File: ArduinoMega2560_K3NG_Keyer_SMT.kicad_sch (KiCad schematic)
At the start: 5 parts, among them J2 Barrel_Jack, J23 Conn_01x02

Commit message: Small drawing cleanups.
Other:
- sheet Misc: file untitled.kicad_sch -> misc.kicad_sch
- note added: "Arduino Mega 2560 clone Microprocessor"
- note added: "Miscellaneous Parts on separate sheets"
- note removed: "Miscellaneous Parts on separate sheet"
- title: Arduino Mega2560 K3NG Morse Code Keyer - SMT version -> Arduino Mega2560 K3NG Keyer - Microprocessor
- moved on the sheet: A1, JP1

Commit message: Changed power jack and LCD symbols.
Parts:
- removed J2: Barrel_Jack, symbol Connector:Barrel_Jack
- added J2: Conn_01x02, symbol Connector_Generic:Conn_01x02
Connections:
- net GND: now also J2.2 (Pin_2)
- net Vin: now also J2.1 (Pin_1)
- net A3 renamed PS2_DATA
- net D3 renamed PS2_CLK
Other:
- note added: "+"
- note added: "GND"
- note removed: "PS/2 Keyboard"
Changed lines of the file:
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@@
   (junction (at 97.79 156.21) (diameter 0) (color 0 0 0 0)
   )
-  (wire (pts (xy 41.91 31.75) (xy 48.26 31.75))
+  (wire (pts (xy 39.37 31.75) (xy 45.72 31.75))
     (stroke (width 0) (type default))
   )
@@
     (stroke (width 0) (type default))
   )
-  (wire (pts (xy 41.91 36.83) (xy 48.26 36.83))
+  (wire (pts (xy 39.37 34.29) (xy 45.72 34.29))
     (stroke (width 0) (type default))
   )
@@
     (stroke (width 0) (type default))
   )
-  (wire (pts (xy 48.26 36.83) (xy 48.26 39.37))
+  (wire (pts (xy 45.72 34.29) (xy 45.72 36.83))
     (stroke (width 0) (type default))
   )
@@
     (effects (font (size 3 3) (thickness 0.6) bold) (justify left bottom))
   )
-  (text "PS/2 Keyboard" (at 170.18 53.34 0)
+  (text "+" (at 30.48 33.02 0)
     (effects (font (size 1.27 1.27)) (justify left bottom))
   )
@@
     (effects (font (size 1.27 1.27)) (justify left bottom))
   )
-  (text "7-12V" (at 20.32 35.56 0)
-    (effects (font (size 1.27 1.27)) (justify left bottom))
+  (text "7-12V" (at 20.32 34.29 0)
+    (effects (font (size 1.27 1.27) (thickness 0.254) bold) (justify left bottom))
   )
   (text "Notes:\n1. Closeing Solder Jumper JP1 allows +5v from Arduino Mega to power the rest of the circuit.\n2. Paddle DIT also connected to D52 for Straight Key."
@@
     (effects (font (size 1.27 1.27)) (justify left bottom))
   )
-  (text "PS/2 Keyboard" (at 77.47 91.44 0)
+  (text "GND" (at 27.94 35.56 0)
     (effects (font (size 1.27 1.27)) (justify left bottom))
   )
@@
     )
   )
+  (global_label "PS2_CLK" (shape input) (at 163.83 52.07 0) (fields_autoplaced)
+    (effects (font (size 1.27 1.27)) (justify left))
+    (property "Intersheetrefs" "${INTERSHEET_REFS}" (at 175.0399 52.07 0)
+      (effects (font (size 1.27 1.27)) (justify left) hide)
+    )
+  )
   (global_label "DIT" (shape input) (at 163.83 57.15 0) (fields_autoplaced)
     (effects (font (size 1.27 1.27)) (justify left))
@@
     )
   )
-  (global_label "D3" (shape input) (at 163.83 52.07 0) (fields_autoplaced)
-    (effects (font (size 1.27 1.27)) (justify left))
-    (property "Intersheetrefs" "${INTERSHEET_REFS}" (at 169.2947 52.07 0)
-      (effects (font (size 1.27 1.27)) (justify left) hide)
-    )
-  )
   (global_label "LCD_RS" (shape input) (at 163.83 120.65 0) (fields_autoplaced)
     (effects (font (size 1.27 1.27)) (justify left))
@@
     )
   )
-  (global_label "A3" (shape input) (at 97.79 90.17 180) (fields_autoplaced)
-    (effects (font (size 1.27 1.27)) (justify right))
-    (property "Intersheetrefs" "${INTERSHEET_REFS}" (at 92.5067 90.17 0)
+  (global_label "PS2_DATA" (shape input) (at 97.79 90.17 180) (fields_autoplaced)
+    (effects (font (size 1.27 1.27)) (justify right))
+    (property "Intersheetrefs" "${INTERSHEET_REFS}" (at 85.7334 90.17 0)
       (effects (font (size 1.27 1.27)) (justify right) hide)
     )
@@
     )
   )
-  (global_label "Vin" (shape input) (at 48.26 31.75 0) (fields_autoplaced)
-    (effects (font (size 1.27 1.27)) (justify left))
-    (property "Intersheetrefs" "${INTERSHEET_REFS}" (at 54.0876 31.75 0)
+  (global_label "Vin" (shape input) (at 45.72 31.75 0) (fields_autoplaced)
+    (effects (font (size 1.27 1.27)) (justify left))
+    (property "Intersheetrefs" "${INTERSHEET_REFS}" (at 51.5476 31.75 0)
       (effects (font (size 1.27 1.27)) (justify left) hide)
     )
@@
     )
   )
-  (symbol (lib_id "power:GND") (at 97.79 163.83 0) (unit 1)
-    (in_bom yes) (on_board yes) (dnp no) (fields_autoplaced)
-    (property "Reference" "#PWR01" (at 97.79 170.18 0)
-      (effects (font (size 1.27 1.27)) hide)
-    )
-    (property "Value" "GND" (at 97.79 168.91 0)
-      (effects (font (size 1.27 1.27)) hide)
-    )
-    (property "Footprint" "" (at 97.79 163.83 0)
-      (effects (font (size 1.27 1.27)) hide)
-    )
-    (property "Datasheet" "" (at 97.79 163.83 0)
-      (effects (font (size 1.27 1.27)) hide)
-    )
-    (pin "1")
-    (instances
-      (project "ArduinoMega2560_K3NG_Keyer_SMT"
-        (path "/9104ccff-1306-44aa-b78d-6ce3da0acd2a"
-          (reference "#PWR01") (unit 1)
-        )
-      )
-    )
-  )
-  (symbol (lib_id "Connector:Barrel_Jack") (at 34.29 34.29 0) (unit 1)
+  (symbol (lib_id "Connector_Generic:Conn_01x02") (at 34.29 31.75 0) (mirror y) (unit 1)
     (in_bom yes) (on_board yes) (dnp no)
     (property "Reference" "J2" (at 34.29 29.21 0)
       (effects (font (size 1.27 1.27)))
     )
-    (property "Value" "Barrel_Jack" (at 34.29 39.37 0)
-      (effects (font (size 1.27 1.27)))
-    )
-    (property "Footprint" "" (at 35.56 35.306 0)
-      (effects (font (size 1.27 1.27)) hide)
-    )
-    (property "Datasheet" "~" (at 35.56 35.306 0)
+    (property "Value" "Conn_01x02" (at 34.29 27.94 0)
+      (effects (font (size 1.27 1.27)) hide)
+    )
+    (property "Footprint" "" (at 34.29 31.75 0)
+      (effects (font (size 1.27 1.27)) hide)
+    )
+    (property "Datasheet" "~" (at 34.29 31.75 0)
       (effects (font (size 1.27 1.27)) hide)
     )
@@
         (path "/9104ccff-1306-44aa-b78d-6ce3da0acd2a"
           (reference "J2") (unit 1)
+        )
+      )
+    )
+  )
+  (symbol (lib_id "power:GND") (at 97.79 163.83 0) (unit 1)
+    (in_bom yes) (on_board yes) (dnp no) (fields_autoplaced)
+    (property "Reference" "#PWR01" (at 97.79 170.18 0)
+      (effects (font (size 1.27 1.27)) hide)
+    )
+    (property "Value" "GND" (at 97.79 168.91 0)
+      (effects (font (size 1.27 1.27)) hide)
+    )
+    (property "Footprint" "" (at 97.79 163.83 0)
+      (effects (font (size 1.27 1.27)) hide)
+    )
+    (property "Datasheet" "" (at 97.79 163.83 0)
+      (effects (font (size 1.27 1.27)) hide)
+    )
+    (pin "1")
+    (instances
+      (project "ArduinoMega2560_K3NG_Keyer_SMT"
+        (path "/9104ccff-1306-44aa-b78d-6ce3da0acd2a"
+          (reference "#PWR01") (unit 1)
         )
       )
@@
     )
   )
-  (symbol (lib_id "power:GND") (at 48.26 39.37 0) (unit 1)
+  (symbol (lib_id "power:GND") (at 45.72 36.83 0) (unit 1)
     (in_bom yes) (on_board yes) (dnp no) (fields_autoplaced)
-    (property "Reference" "#PWR04" (at 48.26 45.72 0)
-      (effects (font (size 1.27 1.27)) hide)
-    )
-    (property "Value" "GND" (at 48.26 44.45 0)
-      (effects (font (size 1.27 1.27)) hide)
-    )
-    (property "Footprint" "" (at 48.26 39.37 0)
-      (effects (font (size 1.27 1.27)) hide)
-    )
-    (property "Datasheet" "" (at 48.26 39.37 0)
-      (effects (font (size 1.27 1.27)) hide)
-    )
+    (property "Reference" "#PWR04" (at 45.72 43.18 0)
+      (effects (font (size 1.27 1.27)) hide)
+    )
+    (property "Value" "GND" (at 45.72 41.91 0)
+      (effects (font (size 1.27 1.27)) hide)
+    )
+    (property "Footprint" "" (at 45.72 36.83 0)
+      (effects (font (size 1.27 1.27)) hide)
+    )
+    (property "Datasheet" "" (at 45.72 36.83 0)
+      (effects (font (size 1.27 1.27)) hide)
+    )

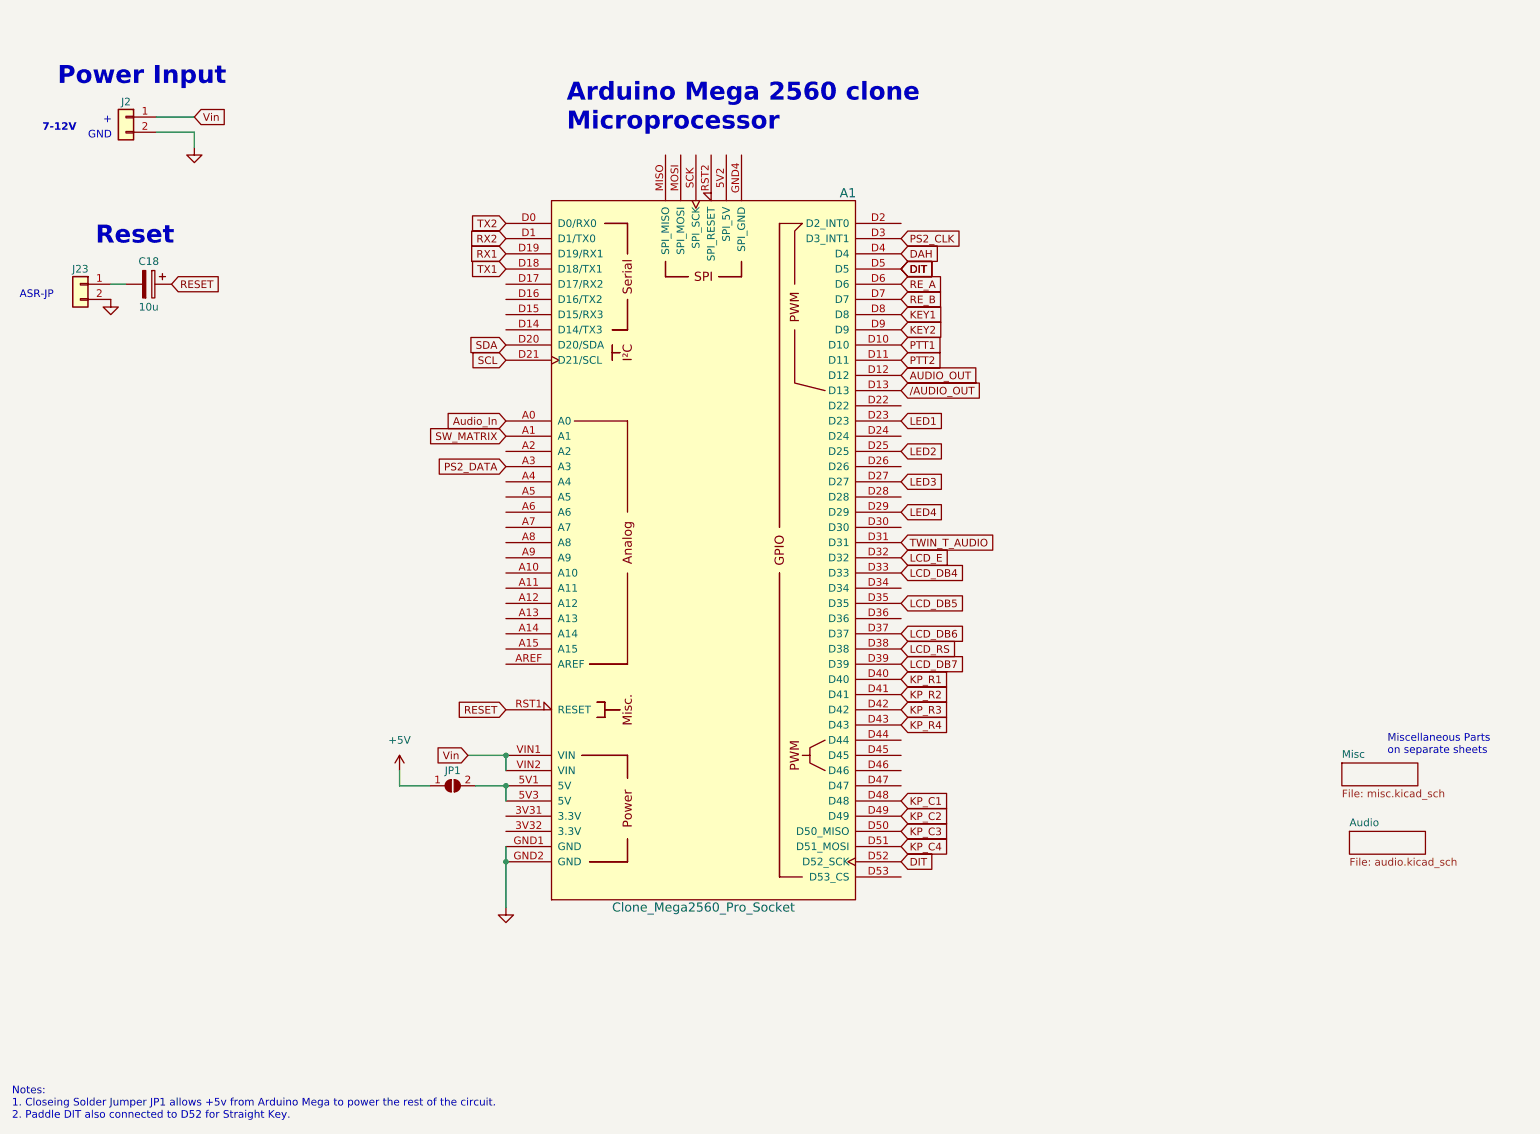
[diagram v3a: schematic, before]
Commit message: Added multi-hole strips to unused pins on Arduino Mega 2560 microprocessor. Also, some minor changes.
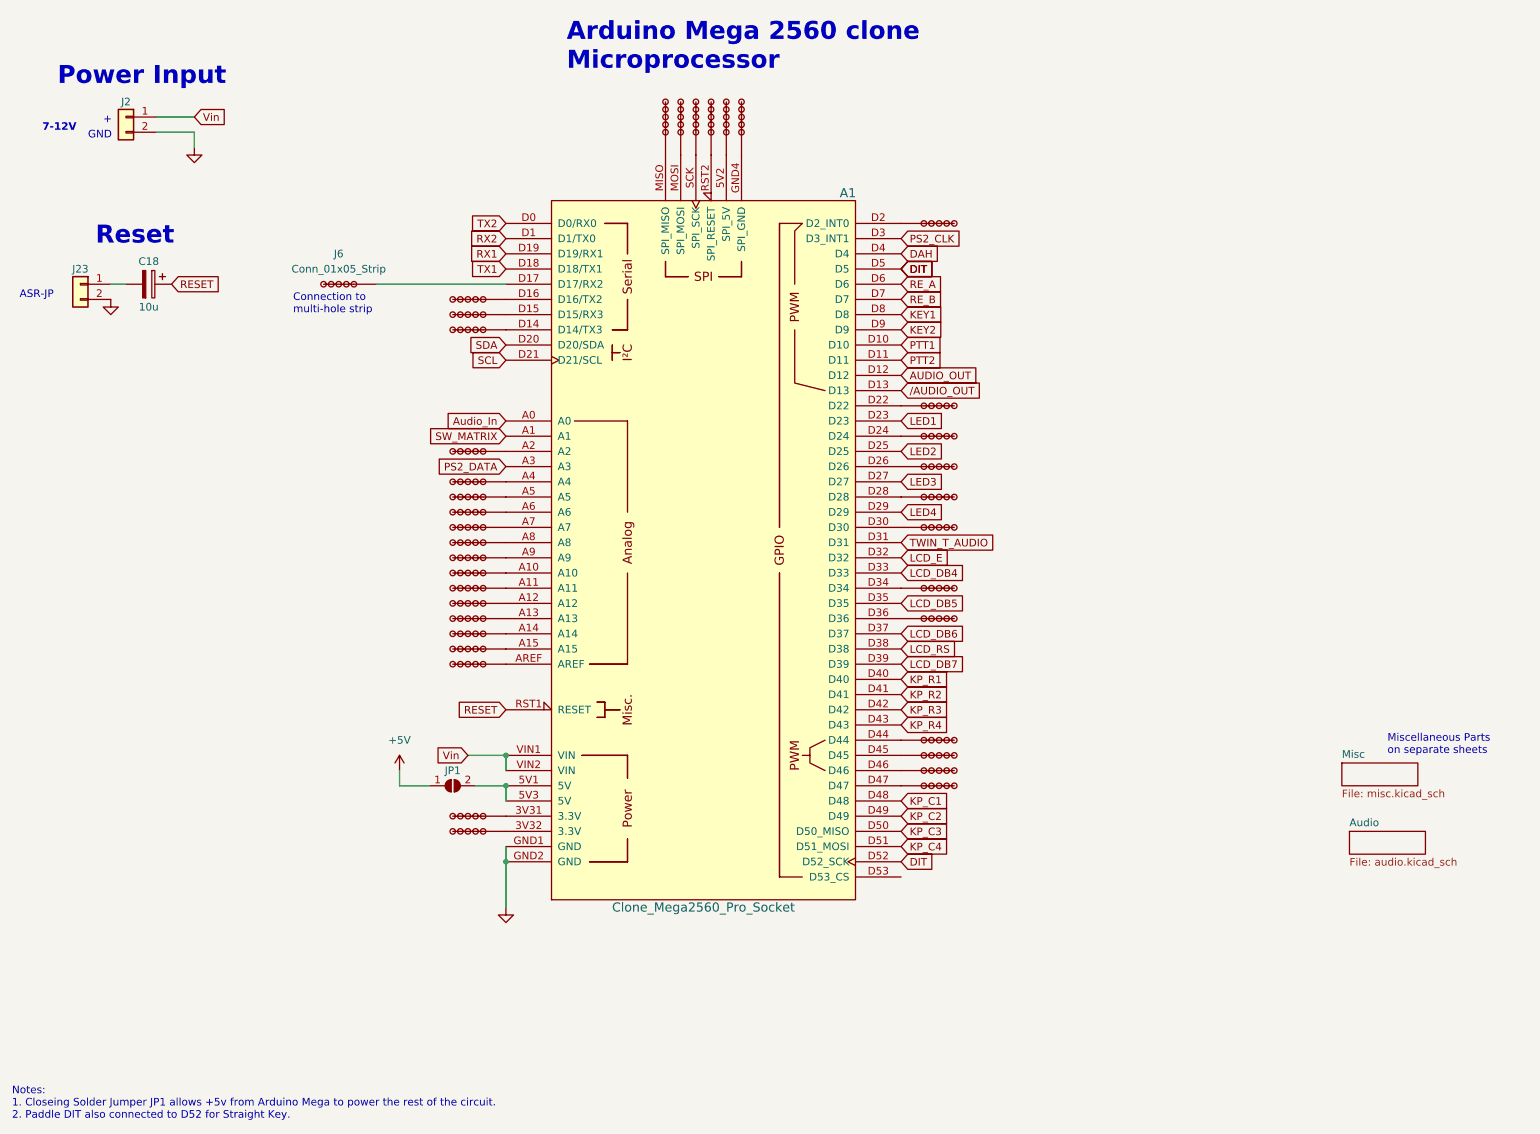
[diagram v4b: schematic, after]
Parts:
- added J10, J11, J12, J13, J25, J26, J27, J28, J29, J30, J31, J32, J33, J34, J35, J36, J37, J38, J39, J40, J41, J42, J43, J44, J45, J46, J47, J48, J49, J50, J51, J52, J53, J54, J6, J7, J8, J9: Conn_01x05_Strip, User:01x05_Strip, symbol User_KICAD6:Conn_01x05_Strip
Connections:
- net at A1.3V31 (3.3V): now also J35. (Pin_1)
- net at A1.3V32 (3.3V): now also J36. (Pin_1)
- net at A1.5V2 (SPI_5V): now also J50. (Pin_1)
- net at A1.A10: now also J28. (Pin_1)
- net at A1.A11: now also J29. (Pin_1)
- net at A1.A12: now also J30. (Pin_1)
- net at A1.A13: now also J31. (Pin_1)
- net at A1.A14: now also J32. (Pin_1)
- net at A1.A15: now also J33. (Pin_1)
- net at A1.A2: now also J10. (Pin_1)
- net at A1.A4: now also J11. (Pin_1)
- net at A1.A5: now also J12. (Pin_1)
- net at A1.A6: now also J13. (Pin_1)
- net at A1.A7: now also J25. (Pin_1)
- net at A1.A8: now also J26. (Pin_1)
- net at A1.A9: now also J27. (Pin_1)
- net at A1.AREF: now also J34. (Pin_1)
- net at A1.D14 (D14/TX3): now also J9. (Pin_1)
- net at A1.D15 (D15/RX3): now also J8. (Pin_1)
- net at A1.D16 (D16/TX2): now also J7. (Pin_1)
- net at A1.D17 (D17/RX2): now also J6. (Pin_1)
- net at A1.D2 (D2_INT0): now also J48. (Pin_1)
- net at A1.D22: now also J47. (Pin_1)
- net at A1.D24: now also J46. (Pin_1)
- net at A1.D26: now also J45. (Pin_1)
- net at A1.D28: now also J44. (Pin_1)
- net at A1.D30: now also J43. (Pin_1)
- net at A1.D34: now also J42. (Pin_1)
- net at A1.D36: now also J41. (Pin_1)
- net at A1.D44: now also J40. (Pin_1)
- net at A1.D45: now also J39. (Pin_1)
- net at A1.D46: now also J38. (Pin_1)
- net at A1.D47: now also J37. (Pin_1)
- net at A1.GND4 (SPI_GND): now also J49. (Pin_1)
- net at A1.MISO (SPI_MISO): now also J54. (Pin_1)
- net at A1.MOSI (SPI_MOSI): now also J53. (Pin_1)
- net at A1.RST2 (SPI_RESET): now also J51. (Pin_1)
- net at A1.SCK (SPI_SCK): now also J52. (Pin_1)
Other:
- note added: "Connection to multi-hole strip"
